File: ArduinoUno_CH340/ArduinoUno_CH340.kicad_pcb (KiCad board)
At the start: 2 copper layers, 68.6 x 53.3 mm, 58 parts, among them J1 Jack_DC, J10 I2C, J11 Servo, J2 USB_B, J3 Header_4P, J4 ICSPx, J5 POWER, J6 IOH, J7 ANALOG, J8 IOL, J9 RxTx, Q1 MOS-P_FDN304P, U1 MC33269-SOT, U2 CH340G, U3 LM358D, U4 ATmega328-P, U5 LP2985-3.3, Y1 16MHz, Y2 16MHz

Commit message: Chamge BMP to PNG
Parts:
- moved R10 33.1 mm to (71.4, 141.2)
- moved R11 33.1 mm to (71.4, 143.5)
- moved U4 33.1 mm to (72.4, 152.8)
- moved U3 32.4 mm to (55.2, 70.8)
- moved R8 31.9 mm to (48.3, 70.6), turned to 180 degrees
- moved R9 30.9 mm to (48.3, 72.7), turned to 180 degrees
- moved C11 19.3 mm to (56.1, 139.9)
- moved D2 19.3 mm to (46.4, 144.8)
- moved C10 15.5 mm to (67.1, 63.2)
- moved LED4 15.5 mm to (80.0, 78.3)
- moved Q1 15.5 mm to (74.9, 70.4)
- moved R12 15.5 mm to (76.1, 82.4)
- moved U5 15.5 mm to (85.6, 94.3)
- moved C13 15.5 mm to (52.7, 60.2)
- moved C12 15.5 mm to (40.3, 71.8)
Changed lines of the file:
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@@
   (net 55 "unconnected-(U5-BP-Pad4)")
   (footprint "02pyzPassive:C_0805_HandSolder" (layer "F.Cu")
-    (at 46.7175 85.96 180)
+    (at 40.3125 71.805 180)
     (descr "Capacitor SMD 0805 (2012 Metric), square (rectangular) end terminal, IPC_7351 nominal with elongated pad for handsoldering. (Body size source: IPC-SM-782 page 76, https://www.pcb-3d.com/wordpress/wp-content/uploads/ipc-sm-782a_amendment_1_and_2.pdf, https://docs.google.com/spreadsheets/d/1BsfQQcO9C6DZCsRaXUlFlo91Tg2WpOkGARC1WS5S8t0/edit?usp=sharing), generated with kicad-footprint-generator")
     (tags "capacitor handsolder")
@@
   )
   (footprint "03pyzActive:SOT-23" (layer "F.Cu")
-    (at 81.2775 84.5175)
+    (at 74.8725 70.3625)
     (descr "SOT, 3 Pin (https://www.jedec.org/system/files/docs/to-236h.pdf variant AB), generated with kicad-footprint-generator ipc_gullwing_generator.py")
     (tags "SOT TO_SOT_SMD")
@@
   )
   (footprint "03pyzActive:LED_D3.0mm" (layer "F.Cu")
-    (at 86.36 92.43 90)
+    (at 79.955 78.275 90)
     (descr "IR-LED, diameter 3.0mm, 2 pins, color: clear")
     (tags "IR infrared LED diameter 3.0mm 2 pins clear")
@@
   )
   (footprint "Package_TO_SOT_SMD:SOT-23-5" (layer "F.Cu")
-    (at 92.025 108.4575 -90)
+    (at 85.62 94.3025 -90)
     (descr "SOT, 5 Pin (https://www.jedec.org/sites/default/files/docs/Mo-178c.PDF variant AA), generated with kicad-footprint-generator ipc_gullwing_generator.py")
     (tags "SOT TO_SOT_SMD")
@@
   )
   (footprint "07pyzIC_MCU:SOIC-8_3.9x4.9mm_P1.27mm" (layer "F.Cu")
-    (at 70.55 99.415)
+    (at 55.245 70.84)
     (descr "SOIC, 8 Pin (JEDEC MS-012AA, https://www.analog.com/media/en/package-pcb-resources/package/pkg_pdf/soic_narrow-r/r_8.pdf), generated with kicad-footprint-generator ipc_gullwing_generator.py")
     (tags "SOIC SO")
@@
   )
   (footprint "02pyzPassive:R_0805_HandSolder" (layer "F.Cu")
-    (at 64.075 99.32 -90)
+    (at 48.26 72.745 180)
     (descr "Resistor SMD 0805 (2012 Metric), square (rectangular) end terminal, IPC_7351 nominal with elongated pad for handsoldering. (Body size source: IPC-SM-782 page 72, https://www.pcb-3d.com/wordpress/wp-content/uploads/ipc-sm-782a_amendment_1_and_2.pdf), generated with kicad-footprint-generator")
     (tags "resistor handsolder")
@@
     (property "ki_keywords" "R res resistor")
     (attr smd)
-    (fp_text reference "R9" (at 3 0 90) (layer "F.SilkS")
-        (effects (font (size 1 1) (thickness 0.15)))
-    )
-    (fp_text value "10K" (at 0 1.65 90) (layer "F.Fab")
-        (effects (font (size 1 1) (thickness 0.15)))
-    )
-    (fp_text user "${REFERENCE}" (at 0 0 90) (layer "F.Fab")
+    (fp_text reference "R9" (at 3 0) (layer "F.SilkS")
+        (effects (font (size 1 1) (thickness 0.15)))
+    )
+    (fp_text value "10K" (at 0 1.65) (layer "F.Fab")
+        (effects (font (size 1 1) (thickness 0.15)))
+    )
+    (fp_text user "${REFERENCE}" (at 0 0) (layer "F.Fab")
         (effects (font (size 0.5 0.5) (thickness 0.08)))
     )
@@
     (fp_line (start 1 0.625) (end -1 0.625)
       (stroke (width 0.1) (type solid)) (layer "F.Fab"))
-    (pad "1" smd roundrect (at -1 0 270) (size 1.2 1.4) (layers "F.Cu" "F.Paste" "F.Mask") (roundrect_rratio 0.208333)
+    (pad "1" smd roundrect (at -1 0 180) (size 1.2 1.4) (layers "F.Cu" "F.Paste" "F.Mask") (roundrect_rratio 0.208333)
       (net 2 "GND") (pintype "passive"))
-    (pad "2" smd roundrect (at 1 0 270) (size 1.2 1.4) (layers "F.Cu" "F.Paste" "F.Mask") (roundrect_rratio 0.208333)
+    (pad "2" smd roundrect (at 1 0 180) (size 1.2 1.4) (layers "F.Cu" "F.Paste" "F.Mask") (roundrect_rratio 0.208333)
       (net 32 "Net-(U3-INPA+)") (pintype "passive"))
     (model "${KICAD6_3DMODEL_DIR}/Resistor_SMD.3dshapes/R_0805_2012Metric.wrl"
@@
   )
   (footprint "03pyzActive:D_1206_HandSolder" (layer "F.Cu")
-    (at 43.3475 163.8775 -90)
+    (at 46.355 144.8425 -90)
     (descr "Capacitor SMD 1206 (3216 Metric), square (rectangular) end terminal, IPC_7351 nominal with elongated pad for handsoldering. (Body size source: IPC-SM-782 page 76, https://www.pcb-3d.com/wordpress/wp-content/uploads/ipc-sm-782a_amendment_1_and_2.pdf), generated with kicad-footprint-generator")
     (tags "capacitor handsolder")
@@
   )
   (footprint "02pyzPassive:C_0805_HandSolder" (layer "F.Cu")
-    (at 59.1125 74.32)
+    (at 52.7075 60.165)
     (descr "Capacitor SMD 0805 (2012 Metric), square (rectangular) end terminal, IPC_7351 nominal with elongated pad for handsoldering. (Body size source: IPC-SM-782 page 76, https://www.pcb-3d.com/wordpress/wp-content/uploads/ipc-sm-782a_amendment_1_and_2.pdf, https://docs.google.com/spreadsheets/d/1BsfQQcO9C6DZCsRaXUlFlo91Tg2WpOkGARC1WS5S8t0/edit?usp=sharing), generated with kicad-footprint-generator")
     (tags "capacitor handsolder")
@@
   )
   (footprint "02pyzPassive:R_0805_HandSolder" (layer "F.Cu")
-    (at 82.47 96.51 -90)
+    (at 76.065 82.355 -90)
     (descr "Resistor SMD 0805 (2012 Metric), square (rectangular) end terminal, IPC_7351 nominal with elongated pad for handsoldering. (Body size source: IPC-SM-782 page 72, https://www.pcb-3d.com/wordpress/wp-content/uploads/ipc-sm-782a_amendment_1_and_2.pdf), generated with kicad-footprint-generator")
     (tags "resistor handsolder")
@@
   )
   (footprint "02pyzPassive:R_0805_HandSolder" (layer "F.Cu")
-    (at 62.075 99.32 -90)
+    (at 48.26 70.57 180)
     (descr "Resistor SMD 0805 (2012 Metric), square (rectangular) end terminal, IPC_7351 nominal with elongated pad for handsoldering. (Body size source: IPC-SM-782 page 72, https://www.pcb-3d.com/wordpress/wp-content/uploads/ipc-sm-782a_amendment_1_and_2.pdf), generated with kicad-footprint-generator")
     (tags "resistor handsolder")
@@
     (property "ki_keywords" "R res resistor")
     (attr smd)
-    (fp_text reference "R8" (at 3.175 0 90) (layer "F.SilkS")
-        (effects (font (size 1 1) (thickness 0.15)))
-    )
-    (fp_text value "10K" (at 0 1.65 90) (layer "F.Fab")
-        (effects (font (size 1 1) (thickness 0.15)))
-    )
-    (fp_text user "${REFERENCE}" (at 0 0 90) (layer "F.Fab")
+    (fp_text reference "R8" (at 3.175 0) (layer "F.SilkS")
+        (effects (font (size 1 1) (thickness 0.15)))
+    )
+    (fp_text value "10K" (at 0 1.65) (layer "F.Fab")
+        (effects (font (size 1 1) (thickness 0.15)))
+    )
+    (fp_text user "${REFERENCE}" (at 0 0) (layer "F.Fab")
         (effects (font (size 0.5 0.5) (thickness 0.08)))
     )
@@
     (fp_line (start 1 0.625) (end -1 0.625)
       (stroke (width 0.1) (type solid)) (layer "F.Fab"))
-    (pad "1" smd roundrect (at -1 0 270) (size 1.2 1.4) (layers "F.Cu" "F.Paste" "F.Mask") (roundrect_rratio 0.208333)
+    (pad "1" smd roundrect (at -1 0 180) (size 1.2 1.4) (layers "F.Cu" "F.Paste" "F.Mask") (roundrect_rratio 0.208333)
       (net 3 "VIN") (pintype "passive"))
-    (pad "2" smd roundrect (at 1 0 270) (size 1.2 1.4) (layers "F.Cu" "F.Paste" "F.Mask") (roundrect_rratio 0.208333)
+    (pad "2" smd roundrect (at 1 0 180) (size 1.2 1.4) (layers "F.Cu" "F.Paste" "F.Mask") (roundrect_rratio 0.208333)
       (net 32 "Net-(U3-INPA+)") (pintype "passive"))
     (model "${KICAD6_3DMODEL_DIR}/Resistor_SMD.3dshapes/R_0805_2012Metric.wrl"
@@
   )
   (footprint "02pyzPassive:C_0805_HandSolder" (layer "F.Cu")
-    (at 53.0875 158.94)
+    (at 56.095 139.905)
     (descr "Capacitor SMD 0805 (2012 Metric), square (rectangular) end terminal, IPC_7351 nominal with elongated pad for handsoldering. (Body size source: IPC-SM-782 page 76, https://www.pcb-3d.com/wordpress/wp-content/uploads/ipc-sm-782a_amendment_1_and_2.pdf, https://docs.google.com/spreadsheets/d/1BsfQQcO9C6DZCsRaXUlFlo91Tg2WpOkGARC1WS5S8t0/edit?usp=sharing), generated with kicad-footprint-generator")
     (tags "capacitor handsolder")
@@
   )
   (footprint "02pyzPassive:R_0805_HandSolder" (layer "F.Cu")
-    (at 63.47 173.38)
+    (at 71.41 141.195)
     (descr "Resistor SMD 0805 (2012 Metric), square (rectangular) end terminal, IPC_7351 nominal with elongated pad for handsoldering. (Body size source: IPC-SM-782 page 72, https://www.pcb-3d.com/wordpress/wp-content/uploads/ipc-sm-782a_amendment_1_and_2.pdf), generated with kicad-footprint-generator")
     (tags "resistor handsolder")
@@
   )
   (footprint "02pyzPassive:C_0805_HandSolder" (layer "F.Cu")
-    (at 73.4825 77.375)
+    (at 67.0775 63.22)
     (descr "Capacitor SMD 0805 (2012 Metric), square (rectangular) end terminal, IPC_7351 nominal with elongated pad for handsoldering. (Body size source: IPC-SM-782 page 76, https://www.pcb-3d.com/wordpress/wp-content/uploads/ipc-sm-782a_amendment_1_and_2.pdf, https://docs.google.com/spreadsheets/d/1BsfQQcO9C6DZCsRaXUlFlo91Tg2WpOkGARC1WS5S8t0/edit?usp=sharing), generated with kicad-footprint-generator")
     (tags "capacitor handsolder")
@@
   )
   (footprint "Package_DIP:DIP-28_W7.62mm" (layer "F.Cu")
-    (at 64.45 184.94 -90)
+    (at 72.39 152.755 -90)
     (descr "28-lead though-hole mounted DIP package, row spacing 7.62 mm (300 mils)")
     (tags "THT DIP DIL PDIP 2.54mm 7.62mm 300mil")
@@
   )
   (footprint "02pyzPassive:R_0805_HandSolder" (layer "F.Cu")
-    (at 63.47 175.695)
+    (at 71.41 143.51)
     (descr "Resistor SMD 0805 (2012 Metric), square (rectangular) end terminal, IPC_7351 nominal with elongated pad for handsoldering. (Body size source: IPC-SM-782 page 72, https://www.pcb-3d.com/wordpress/wp-content/uploads/ipc-sm-782a_amendment_1_and_2.pdf), generated with kicad-footprint-generator")
     (tags "resistor handsolder")

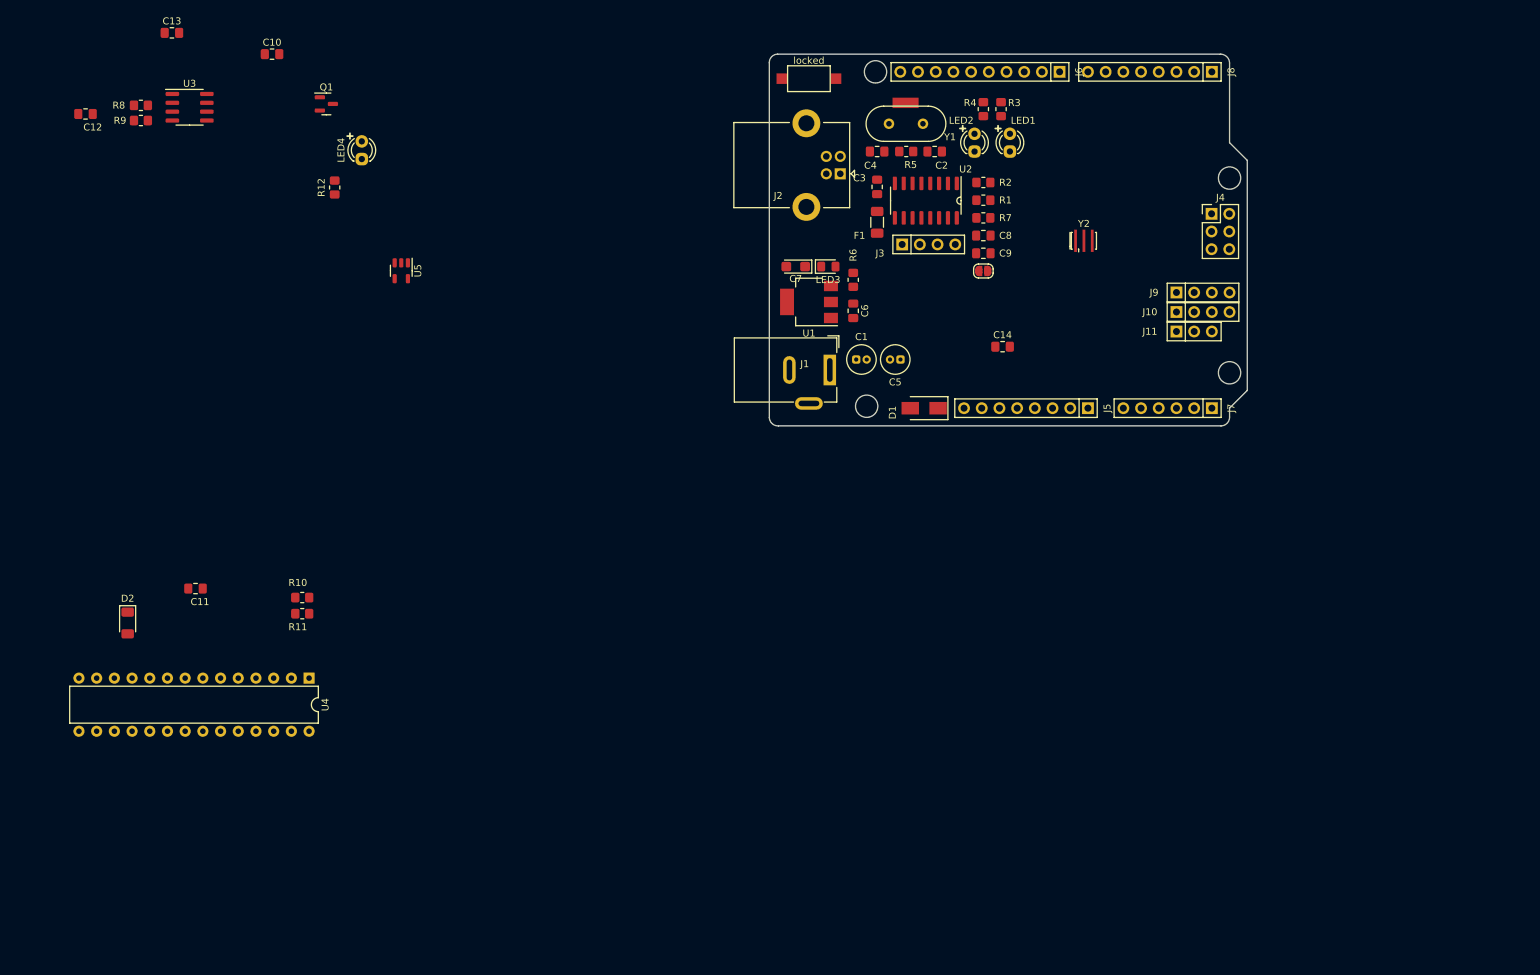
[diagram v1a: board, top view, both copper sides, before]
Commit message: Complete Arduino Uno CH340
Complete Project Arduino uno CH340
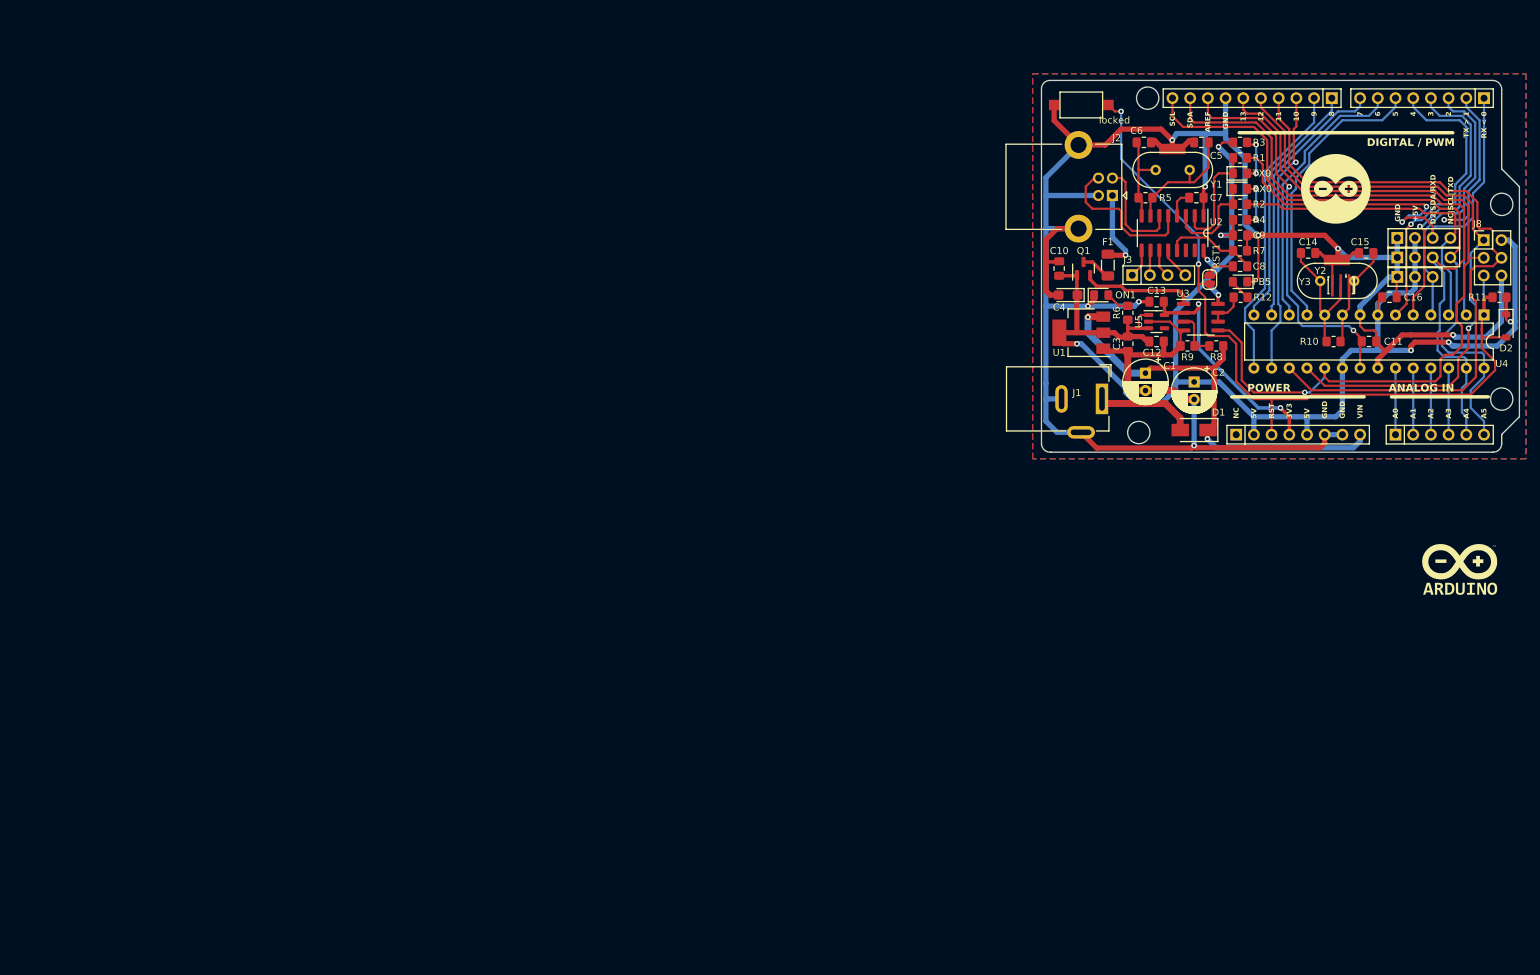
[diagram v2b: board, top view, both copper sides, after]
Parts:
- added C14: 22pF, 02pyzPassive:C_0805_HandSolder, F.Cu at (215.7, 91.8)
- added C15: 22pF, 02pyzPassive:C_0805_HandSolder, F.Cu at (224.1, 91.8)
- added G***: LOGO, 00pyzLogo:Arduino-01, F.Cu at (237.5, 137.2)
- added G***: LOGO, 00pyzLogo:Arduino-02, F.Cu at (219.7, 82.5)
- added Y3: 16MHz, 02pyzPassive:Crystal_HC49-4H_Vertical_GND, F.Cu at (222.4, 95.8)
- C1: footprint 02pyzPassive:C_Radial_D4.0mm_H5.0mm_P1.50mm -> 02pyzPassive:C_Radial_D6.3mm_P2.50mm
- C2: renamed from C5; footprint 02pyzPassive:C_Radial_D4.0mm_H5.0mm_P1.50mm -> 02pyzPassive:C_Radial_D6.3mm_P2.50mm
- D2: value CD1206-S01575 -> 1N4148; footprint 03pyzActive:D_1206_HandSolder -> 03pyzActive:D_SOD-123
- ON1: renamed from LED3; footprint 03pyzActive:D_0805_HandSolder -> 03pyzActive:LED_0805_HandSolder
- PB5: renamed from LED4; footprint 03pyzActive:LED_D3.0mm -> 03pyzActive:LED_0805_HandSolder
- RX0: renamed from LED2; footprint 03pyzActive:LED_D3.0mm -> 03pyzActive:LED_0805_HandSolder
- TX0: renamed from LED1; footprint 03pyzActive:LED_D3.0mm -> 03pyzActive:LED_0805_HandSolder
- moved D2 202.3 mm to (244.2, 102.2)
- moved R11 177.7 mm to (243.2, 98.1), turned to 180 degrees
- moved U4 176.5 mm to (241.0, 100.6)
- moved C16 176.3 mm to (227.4, 98.1)
- moved R8 158.1 mm to (202.6, 105.1)
- moved C12 157.1 mm to (194.0, 104.5), turned to 0 degrees
- moved R9 153.6 mm to (198.4, 105.1), turned to 0 degrees
- moved R10 152.5 mm to (219.4, 104.5), turned to 180 degrees
- moved U3 148.2 mm to (200.3, 101.0)
- moved C13 146.5 mm to (194.0, 98.7), turned to 180 degrees
- moved R12 130.9 mm to (206.1, 98.1), turned to 0 degrees
- moved PB5 127.2 mm to (206.0, 95.9), turned to 180 degrees
- moved C10 117.1 mm to (180.0, 94.0), turned to 90 degrees
- moved Q1 111.2 mm to (183.5, 94.0), turned to 90 degrees
- moved U5 108.6 mm to (194.0, 101.6), turned to 0 degrees
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- renumbered C14 to C11, C11 to C16, C6 to C3, C7 to C4, C3 to C5, C4 to C6, C2 to C7, J7 to J10, J8 to J11, J9 to J4, J10 to J5, J11 to J6, J5 to J7, J4 to J8, J6 to J9, SOL1 to RST1
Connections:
- net Net-(U4-PB6(PCINT6/XTAL1/TOSC1)) renamed /XT1
- net Net-(U4-PB7(PCINT7/XTAL2/TOSC2)) renamed /XT2
- J11 pad 3: Net-(J8-Pin_3) -> /Servo
- J11 pad 6: /Servo -> Net-(J11-Pin_6)
- U2 pad 11: Net-(J3-Pin_4) -> Net-(J3-Pin_3)
- U2 pad 12: Net-(J3-Pin_3) -> Net-(J3-Pin_4)
- U4 pad 11: /Servo -> Net-(J11-Pin_6)
- U4 pad 4: Net-(J8-Pin_3) -> /Servo
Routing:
- net GND: track 0.00 -> 351.0 mm, vias 0 -> 8
- net +5V: track 0.00 -> 217.8 mm, vias 0 -> 8
- net /ICSP_RST: track 0.00 -> 118.0 mm, vias 0 -> 2
- net /ICSP_SCLK: track 0.00 -> 115.0 mm, vias 0 -> 1
- net /ICSP_MOSI: track 0.00 -> 99.3 mm
- net /I2C_SDA: track 0.00 -> 94.3 mm
- net /I2C_SCL: track 0.00 -> 93.4 mm
- net /ICSP_MISO: track 0.00 -> 91.3 mm, vias 0 -> 1
- net /M8_RXD: track 0.00 -> 79.9 mm, vias 0 -> 2
- net /M8_TXD: track 0.00 -> 69.9 mm, vias 0 -> 1
- net VIN: track 0.00 -> 63.3 mm, vias 0 -> 2
- net /AREF: track 0.00 -> 56.1 mm, vias 0 -> 2
- net Net-(J9-Pin_2): track 0.00 -> 43.4 mm
- net Net-(J11-Pin_5): track 0.00 -> 43.1 mm, vias 0 -> 1
- net Net-(J11-Pin_6): track 0.00 -> 41.6 mm
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- added copper zone on B.Cu, net (none)
- added copper zone on F.Cu, net (none)
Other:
- board text added: "+5V"
- board text added: "10"
- board text added: "11"
- board text added: "12"
- board text added: "13"
- board text added: "2"
- board text added: "3"
- board text added: "3V3"
- board text added: "4"
- board text added: "5"
- board text added: "5V"
- board text added: "6"
- board text added: "7"
- board text added: "8"
- board text added: "9"
- board text added: "A0"
- board text added: "A1"
- board text added: "A2"
- board text added: "A3"
- board text added: "A4"
- board text added: "A5"
- board text added: "ANALOG IN"
- board text added: "AREF"
- board text added: "D2|SDA/RXD"
- board text added: "DIGITAL / PWM"
- board text added: "GND"
- board text added: "NC"
- board text added: "NC|SCL|TXD"
- board text added: "POWER"
- board text added: "RST"
- board text added: "RX < 0"
- board text added: "SCL"
- board text added: "SDA"
- board text added: "TX > 1"
- board text added: "VIN"
- board text added: "locked"
